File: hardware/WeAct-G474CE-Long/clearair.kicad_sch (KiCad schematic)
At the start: 40 parts, among them J1 220VAC mains in, M1 AC vent fan, M2 40mm fan (5V or 12V), Q1 2N7000, Q2 2N7000, Q3 2N2222A, Q4 IRFZ44N, Q5 AO3400A, SW1 RESET, SW2 COLD_BOOT, U1 SPS30, U2 BME680, U3 MQ131, U4 MiCS-4514, U5 RobotDyn AC dimmer, U6 PCF8563 RTC

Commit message: define the buzzer cycle
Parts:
- removed Q4: IRFZ44N, Package_TO_SOT_THT:TO-220-3_Vertical, symbol Transistor_FET:IRLZ44N
- removed R16: 10k, symbol Device:R
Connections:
- net at Q3.3 (C): now also BZ1.2 (-)
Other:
- note added: "Buzzer: PB15 (BUZZER_IN) -> R9 1k -> Q3 2N2222A base. Q3 switches the 12V buzzer on its low side: PB15 HIGH -> buzzer ON, LOW -> OFF. MiCS-4514 PRE tied to GND (boost not used). PB12 (MQ131_PREHEAT) -> R17 100R -> Q5 AO3400A gate, R18 100k pull-down: low-side switch in the MQ131 GND, HIGH = heater on. Cold/warm boot button SW2 -> PB14 (BOOT_MODE, pull-up). Gate PB1 (TRIAC_DIMMER) -> RobotDyn PSM."
- note removed: "Buzzer: PB15 (BUZZER_IN) -> R9 -> Q3. Q3 inverts: PB15 HIGH -> buzzer OFF; LOW -> R16 pulls IRFZ44N gate to 12V -> buzzer ON. MiCS-4514 PRE tied to GND (boost not used). PB12 (MQ131_PREHEAT) -> R17 100R -> Q5 AO3400A gate, R18 100k pull-down: low-side switch in the MQ131 GND, HIGH = heater on. Cold/warm boot button SW2 -> PB14 (BOOT_MODE, pull-up). Gate PB1 (TRIAC_DIMMER) -> RobotDyn PSM."
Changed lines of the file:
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@@
 		(pin "3")
 		(instances (project "clearair" (path "/953560a5-36cf-5251-8f8d-509802d70a69" (reference "Q3") (unit 1)))))
-	(symbol (lib_id "Device:R") (at 193.04 86.36 180) (unit 1)
-		(exclude_from_sim no) (in_bom yes) (on_board yes) (dnp no)
-		(property "Reference" "R16" (at 195.072 86.36 90) (effects (font (size 1.27 1.27))))
-		(property "Value" "10k" (at 193.04 86.36 90) (effects (font (size 1.27 1.27))))
-		(property "Footprint" "" (at 194.818 86.36 90) (effects (font (size 1.27 1.27)) (hide yes)))
-		(property "Datasheet" "" (at 193.04 86.36 0) (effects (font (size 1.27 1.27)) (hide yes)))
-		(property "Description" "Resistor" (at 193.04 86.36 0) (effects (font (size 1.27 1.27)) (hide yes)))
-		(property "ki_keywords" "R res resistor" (at 193.04 86.36 0) (effects (font (size 1.27 1.27)) (hide yes)))
-		(property "ki_fp_filters" "R_*" (at 193.04 86.36 0) (effects (font (size 1.27 1.27)) (hide yes)))
-		(pin "1")
-		(pin "2")
-		(instances (project "clearair" (path "/953560a5-36cf-5251-8f8d-509802d70a69" (reference "R16") (unit 1)))))
-	(symbol (lib_id "Transistor_FET:IRLZ44N") (at 205.74 76.2 0) (unit 1)
-		(exclude_from_sim no) (in_bom yes) (on_board yes) (dnp no)
-		(property "Reference" "Q4" (at 210.82 74.295 0) (effects (font (size 1.27 1.27))))
-		(property "Value" "IRFZ44N" (at 210.82 76.2 0) (effects (font (size 1.27 1.27))))
-		(property "Footprint" "Package_TO_SOT_THT:TO-220-3_Vertical" (at 210.82 78.105 0) (effects (font (size 1.27 1.27)) (hide yes)))
-		(property "Datasheet" "http://www.irf.com/product-info/datasheets/data/irlz44n.pdf" (at 210.82 80.01 0) (effects (font (size 1.27 1.27)) (hide yes)))
-		(property "Description" "47A Id, 55V Vds, 22mOhm Rds Single N-Channel HEXFET Power MOSFET, TO-220AB" (at 205.74 76.2 0) (effects (font (size 1.27 1.27)) (hide yes)))
-		(property "ki_keywords" "N-Channel HEXFET MOSFET Logic-Level" (at 205.74 76.2 0) (effects (font (size 1.27 1.27)) (hide yes)))
-		(property "ki_fp_filters" "TO?220*" (at 205.74 76.2 0) (effects (font (size 1.27 1.27)) (hide yes)))
-		(pin "1")
-		(pin "2")
-		(pin "3")
-		(instances (project "clearair" (path "/953560a5-36cf-5251-8f8d-509802d70a69" (reference "Q4") (unit 1)))))
 	(symbol (lib_id "Device:Buzzer") (at 213.36 63.5 0) (unit 1)
 		(exclude_from_sim no) (in_bom yes) (on_board yes) (dnp no)
@@
 	(wire (pts (xy 281.94 299.72) (xy 281.94 223.52)) (stroke (width 0) (type default)))
 	(wire (pts (xy 177.8 76.2) (xy 173.99 76.2)) (stroke (width 0) (type default)))
-	(wire (pts (xy 193.04 82.55) (xy 193.04 76.2)) (stroke (width 0) (type default)))
-	(wire (pts (xy 193.04 76.2) (xy 193.04 69.85)) (stroke (width 0) (type default)))
-	(wire (pts (xy 193.04 69.85) (xy 185.42 69.85)) (stroke (width 0) (type default)))
-	(wire (pts (xy 185.42 69.85) (xy 185.42 71.12)) (stroke (width 0) (type default)))
-	(wire (pts (xy 200.66 76.2) (xy 193.04 76.2)) (stroke (width 0) (type default)))
-	(wire (pts (xy 208.28 71.12) (xy 208.28 66.04)) (stroke (width 0) (type default)))
-	(wire (pts (xy 208.28 66.04) (xy 210.82 66.04)) (stroke (width 0) (type default)))
 	(wire (pts (xy 345.44 172.72) (xy 345.44 181.61)) (stroke (width 0) (type default)))
 	(wire (pts (xy 345.44 181.61) (xy 345.44 182.88)) (stroke (width 0) (type default)))
@@
 	(wire (pts (xy 482.6 60.96) (xy 482.6 68.58)) (stroke (width 0) (type default)))
 	(wire (pts (xy 482.6 68.58) (xy 477.52 68.58)) (stroke (width 0) (type default)))
-	(wire (pts (xy 193.04 90.17) (xy 193.04 101.6)) (stroke (width 0) (type default)))
 	(wire (pts (xy 256.54 81.28) (xy 256.54 101.6)) (stroke (width 0) (type default)))
 	(wire (pts (xy 210.82 60.96) (xy 198.12 60.96)) (stroke (width 0) (type default)))
@@
 	(wire (pts (xy 266.7 83.82) (xy 266.7 106.68)) (stroke (width 0) (type default)))
 	(wire (pts (xy 185.42 81.28) (xy 185.42 106.68)) (stroke (width 0) (type default)))
-	(wire (pts (xy 208.28 81.28) (xy 208.28 106.68)) (stroke (width 0) (type default)))
 	(wire (pts (xy 302.26 299.72) (xy 302.26 294.64)) (stroke (width 0) (type default)))
 	(wire (pts (xy 302.26 294.64) (xy 311.15 294.64)) (stroke (width 0) (type default)))
@@
 	(wire (pts (xy 480.06 259.08) (xy 480.06 327.66)) (stroke (width 0) (type default)))
 	(wire (pts (xy 482.6 259.08) (xy 480.06 259.08)) (stroke (width 0) (type default)))
-	(junction (at 193.04 101.6) (diameter 0) (color 0 0 0 0))
 	(junction (at 198.12 101.6) (diameter 0) (color 0 0 0 0))
 	(junction (at 256.54 101.6) (diameter 0) (color 0 0 0 0))
@@
 	(junction (at 313.69 241.3) (diameter 0) (color 0 0 0 0))
 	(junction (at 185.42 106.68) (diameter 0) (color 0 0 0 0))
-	(junction (at 208.28 106.68) (diameter 0) (color 0 0 0 0))
 	(junction (at 266.7 106.68) (diameter 0) (color 0 0 0 0))
 	(junction (at 341.63 106.68) (diameter 0) (color 0 0 0 0))
@@
 	(junction (at 259.08 180.34) (diameter 0) (color 0 0 0 0))
 	(junction (at 226.06 182.88) (diameter 0) (color 0 0 0 0))
-	(junction (at 193.04 76.2) (diameter 0) (color 0 0 0 0))
 	(junction (at 345.44 181.61) (diameter 0) (color 0 0 0 0))
 	(junction (at 363.22 185.42) (diameter 0) (color 0 0 0 0))
@@
 	(text "I2C1: PA15 SCL / PB7 SDA. SPS30 SEL=GND (I2C, 0x69); BME680 SDO=3V3 (0x77), CS=3V3; PCF8563 RTC HW-689 (0x51, CR1220, COT and INT unused). 4k7 pull-ups to 3V3." (exclude_from_sim no) (at 25.4 345.44 0) (effects (font (size 1.27 1.27)) (justify left top)))
 	(text "5V outputs -> 1k8 (series) / 3k3 (to GND) divider -> 3.24V max at MCU pin:\nMQ131 AO -> PA0 (ADC1_IN1), MiCS RED -> PA1 (ADC2_IN2), MiCS NOX -> PA7 (ADC2_IN4), RobotDyn Z-C -> PB0 (EXTI0)." (exclude_from_sim no) (at 25.4 350.52 0) (effects (font (size 1.27 1.27)) (justify left top)))
-	(text "Buzzer: PB15 (BUZZER_IN) -> R9 -> Q3. Q3 inverts: PB15 HIGH -> buzzer OFF; LOW -> R16 pulls IRFZ44N gate to 12V -> buzzer ON.\nMiCS-4514 PRE tied to GND (boost not used). PB12 (MQ131_PREHEAT) -> R17 100R -> Q5 AO3400A gate, R18 100k pull-down: low-side switch in the MQ131 GND, HIGH = heater on. Cold/warm boot button SW2 -> PB14 (BOOT_MODE, pull-up). Gate PB1 (TRIAC_DIMMER) -> RobotDyn PSM." (exclude_from_sim no) (at 25.4 358.14 0) (effects (font (size 1.27 1.27)) (justify left top)))
+	(text "Buzzer: PB15 (BUZZER_IN) -> R9 1k -> Q3 2N2222A base. Q3 switches the 12V buzzer on its low side: PB15 HIGH -> buzzer ON, LOW -> OFF.\nMiCS-4514 PRE tied to GND (boost not used). PB12 (MQ131_PREHEAT) -> R17 100R -> Q5 AO3400A gate, R18 100k pull-down: low-side switch in the MQ131 GND, HIGH = heater on. Cold/warm boot button SW2 -> PB14 (BOOT_MODE, pull-up). Gate PB1 (TRIAC_DIMMER) -> RobotDyn PSM." (exclude_from_sim no) (at 25.4 358.14 0) (effects (font (size 1.27 1.27)) (justify left top)))
 	(text "J2 = STLINK-V3MINIE STDC14: 3 T_VCC, 4 SWDIO, 5/7/11 GND, 6 SWCLK, 12 T_NRST, 13 T_VCP_RX, 14 T_VCP_TX; 1/2/8/9/10 unused.\nSWD goes to the board P5 header (SWCLK/SWDIO/3V3/GND). USART2 VCP: PA2 TX -> T_VCP_TX, PA3 RX <- T_VCP_RX.\nUSART3 (future Arduino link): PB10 TX / PB11 RX through 2N7000 level shifters Q1/Q2." (exclude_from_sim no) (at 25.4 365.76 0) (effects (font (size 1.27 1.27)) (justify left top)))
 	(text "220VAC mains split: J1 -> RobotDyn TRIAC (fan) and PS1 AC-DC (12V buzzer, 5V board + peripherals).\nPS1 pins: 1 L, 2 N, 3 +12V, 4 +5V, 5 GND. M2 40mm fan runs all the time. JP1: bridge 1-2 for a 5V fan, 2-3 for a 12V fan." (exclude_from_sim no) (at 25.4 375.92 0) (effects (font (size 1.27 1.27)) (justify left top)))
@@
 	(junction (at 388.62 215.9) (diameter 0) (color 0 0 0 0))
 	(junction (at 367.03 201.93) (diameter 0) (color 0 0 0 0))
+	(wire (pts (xy 185.42 71.12) (xy 185.42 66.04)) (stroke (width 0) (type default)))
+	(wire (pts (xy 185.42 66.04) (xy 210.82 66.04)) (stroke (width 0) (type default)))
 	(sheet_instances (path "/" (page "1")))
 	(embedded_fonts no)

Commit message: REMOVE PB12 and update files
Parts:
- removed JP1: FAN_V_SEL, symbol Jumper:Jumper_3_Open
- removed M2: 40mm fan (5V or 12V), symbol Motor:Fan
- removed Q5: AO3400A, Package_TO_SOT_SMD:SOT-23, symbol Transistor_FET:AO3400A
- removed R17: 100, symbol Device:R
- removed R18: 100k, symbol Device:R
- added M2: 80mm fan front, Connector_PinHeader_2.54mm:PinHeader_1x04_P2.54mm_Vertical, symbol Connector_Generic:Conn_01x04
- added M3: 80mm fan rear, Connector_PinHeader_2.54mm:PinHeader_1x04_P2.54mm_Vertical, symbol Connector_Generic:Conn_01x04
- added R19, R20: 1k, Resistor_THT:R_Axial_DIN0207_L6.3mm_D2.5mm_P7.62mm_Horizontal, symbol Device:R
- added R21, R22: 10k, Resistor_THT:R_Axial_DIN0207_L6.3mm_D2.5mm_P7.62mm_Horizontal, symbol Device:R
- BZ1: footprint (none) -> Connector_PinHeader_2.54mm:PinHeader_1x02_P2.54mm_Vertical
- J: footprint (none) -> Connector_PinHeader_1.27mm:PinHeader_2x07_P1.27mm_Vertical
- J1, M1: footprint (none) -> TerminalBlock_Phoenix:TerminalBlock_Phoenix_MKDS-1,5-2-5.08_1x02_P5.08mm_Horizontal
- PS1: value AC-DC PSU 220VAC -> 12V / 5V -> AC-DC PSUs 12V 2A + 5V 2A (DC out); footprint (none) -> libraries:PSU_DC_12V_5V_Inputs
- R1, R10, R11, R12, R13, R14, R15, R2, R3, R4, R5, R6, R7, R8, R9: footprint (none) -> Resistor_THT:R_Axial_DIN0207_L6.3mm_D2.5mm_P7.62mm_Horizontal
- SW1, SW2: footprint (none) -> Button_Switch_THT:SW_PUSH_6mm
- U5: footprint (none) -> libraries:RobotDyn_Dimmer_Logic
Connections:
- net +12V: now also M2.2 (Pin_2), M3.2 (Pin_2)
- net +3V3: now also R21.1, R22.1
- net GND: now also U3.2 (GND), M2.1 (Pin_1), M3.1 (Pin_1)
- net at A.14 (PA9): now also R20.2
- net at A.15 (PA8): now also R19.2
- net at A.30 (PA5): now also M2.3 (Pin_3), R21.2
- net at A.7 (PB3): now also M3.3 (Pin_3), R22.2
- new net: M3.4 (Pin_4), R20.1
- new net: M2.4 (Pin_4), R19.1
- no-connect marks 55 -> 52
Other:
- note added: "220VAC mains split: J1 -> RobotDyn TRIAC (fan) and two separate AC-DC supplies (12V 2A: buzzer + M2/M3 fans, 5V 2A: board + peripherals). Off board (on_board no): J1, M1 and the AC side of PS1 and U5, wired with 1.5 mm2 copper. PS1 pins: 1 L, 2 N, 3 +12V, 4 +5V, 5 GND; the DC pins go to two 2-pin headers. U5 logic pins 1-4 go to a 4-pin header. Fans M2 (front) and M3 (rear) are 12V 4-pin 80 mm: 1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"
- note added: "Buzzer: PB15 (BUZZER_IN) -> R9 1k -> Q3 2N2222A base. Q3 switches the 12V buzzer on its low side: PB15 HIGH -> buzzer ON, LOW -> OFF. MiCS-4514 PRE tied to GND (boost not used). MQ131 heater runs on a steady 5 V (VCC/GND straight to the rails, no switch); PB12 is unused. Cold/warm boot button SW2 -> PB14 (BOOT_MODE, pull-up). Gate PB1 (TRIAC_DIMMER) -> RobotDyn PSM."
- note removed: "220VAC mains split: J1 -> RobotDyn TRIAC (fan) and PS1 AC-DC (12V buzzer, 5V board + peripherals). PS1 pins: 1 L, 2 N, 3 +12V, 4 +5V, 5 GND. M2 40mm fan runs all the time. JP1: bridge 1-2 for a 5V fan, 2-3 for a 12V fan."
- note removed: "Buzzer: PB15 (BUZZER_IN) -> R9 1k -> Q3 2N2222A base. Q3 switches the 12V buzzer on its low side: PB15 HIGH -> buzzer ON, LOW -> OFF. MiCS-4514 PRE tied to GND (boost not used). PB12 (MQ131_PREHEAT) -> R17 100R -> Q5 AO3400A gate, R18 100k pull-down: low-side switch in the MQ131 GND, HIGH = heater on. Cold/warm boot button SW2 -> PB14 (BOOT_MODE, pull-up). Gate PB1 (TRIAC_DIMMER) -> RobotDyn PSM."

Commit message: remove onboard parts
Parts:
- removed U1: SPS30, libraries:SPS30, symbol FullModules:SPS30
- removed U2: BME680, libraries:BME680_Board, symbol FullModules:BME680_Board
- removed U3: MQ131, libraries:MQ131_FlyingFish, symbol FullModules:MQ131_FlyingFish
- removed U4: MiCS-4514, libraries:MICS4514_Module, symbol FullModules:MICS4514_Module
- added J3: SPS30 wire header (1 VDD, 2 SDA, 3 SCL, 4 SEL, 5 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, Connector_PinHeader_2.54mm:PinHeader_1x05_P2.54mm_Vertical, symbol Connector_Generic:Conn_01x05
- added J4: BME680 wire header (1 VCC, 2 GND, 3 SCL, 4 SDA, 5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, Connector_PinHeader_2.54mm:PinHeader_1x06_P2.54mm_Vertical, symbol Connector_Generic:Conn_01x06
- added J5: MQ131 wire header (1 VCC, 2 GND, 3 DO nc, 4 AO), Connector_PinHeader_2.54mm:PinHeader_1x04_P2.54mm_Vertical, symbol Connector_Generic:Conn_01x04
- added J6: MiCS-4514 wire header (1 VCC, 2 GND, 3 RED, 4 NOX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, Connector_PinHeader_2.54mm:PinHeader_1x05_P2.54mm_Vertical, symbol Connector_Generic:Conn_01x05
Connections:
- net +3V3: now also J4.1 (Pin_1), J4.5 (Pin_5), J4.6 (Pin_6)
- net +5V: now also J3.1 (Pin_1), J5.1 (Pin_1), J6.1 (Pin_1)
- net GND: now also J3.4 (Pin_4), J3.5 (Pin_5), J4.2 (Pin_2), J5.2 (Pin_2), J6.2 (Pin_2), J6.5 (Pin_5)
- net at A.10 (PA15), R1.2, U6.4 (SCL): now also J3.3 (Pin_3), J4.3 (Pin_3)
- net at A.3 (PB7), R2.2, U6.3 (SDA): now also J3.2 (Pin_2), J4.4 (Pin_4)
- net at R7.1: now also J6.4 (Pin_4)
- net at R5.2: now also J6.3 (Pin_3)
- net at R3.1: now also J5.4 (Pin_4)
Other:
- note added: "220VAC mains split: J1 -> RobotDyn TRIAC (fan) and two separate AC-DC supplies (12V 2A: buzzer + M2/M3 fans, 5V 2A: board + peripherals). Off board (on_board no): J1, M1 and the AC side of PS1 and U5, wired with 1.5 mm2 copper. The sensor modules (SPS30, BME680, MQ131, MiCS-4514) are off the PCB and are connected with wires to the PCB wire headers J3 (SPS30), J4 (BME680), J5 (MQ131) and J6 (MiCS-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"
- note removed: "220VAC mains split: J1 -> RobotDyn TRIAC (fan) and two separate AC-DC supplies (12V 2A: buzzer + M2/M3 fans, 5V 2A: board + peripherals). Off board (on_board no): J1, M1 and the AC side of PS1 and U5, wired with 1.5 mm2 copper. PS1 pins: 1 L, 2 N, 3 +12V, 4 +5V, 5 GND; the DC pins go to two 2-pin headers. U5 logic pins 1-4 go to a 4-pin header. Fans M2 (front) and M3 (rear) are 12V 4-pin 80 mm: 1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"

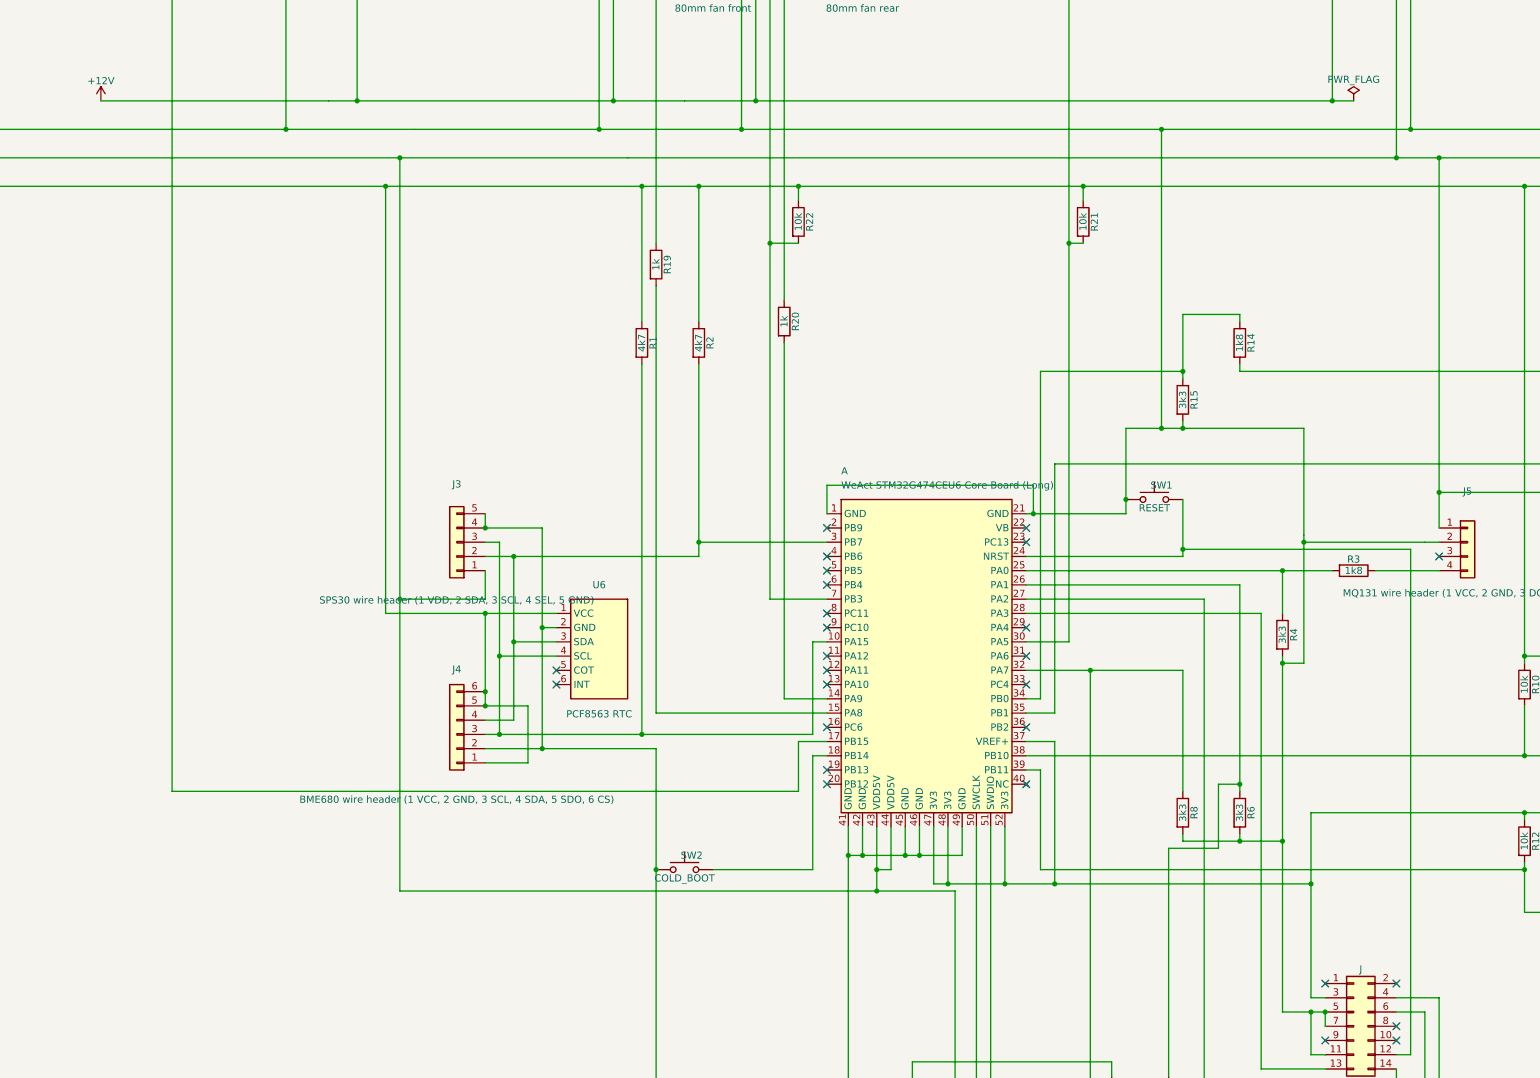
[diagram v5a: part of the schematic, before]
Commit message: validate all needed on the pcb
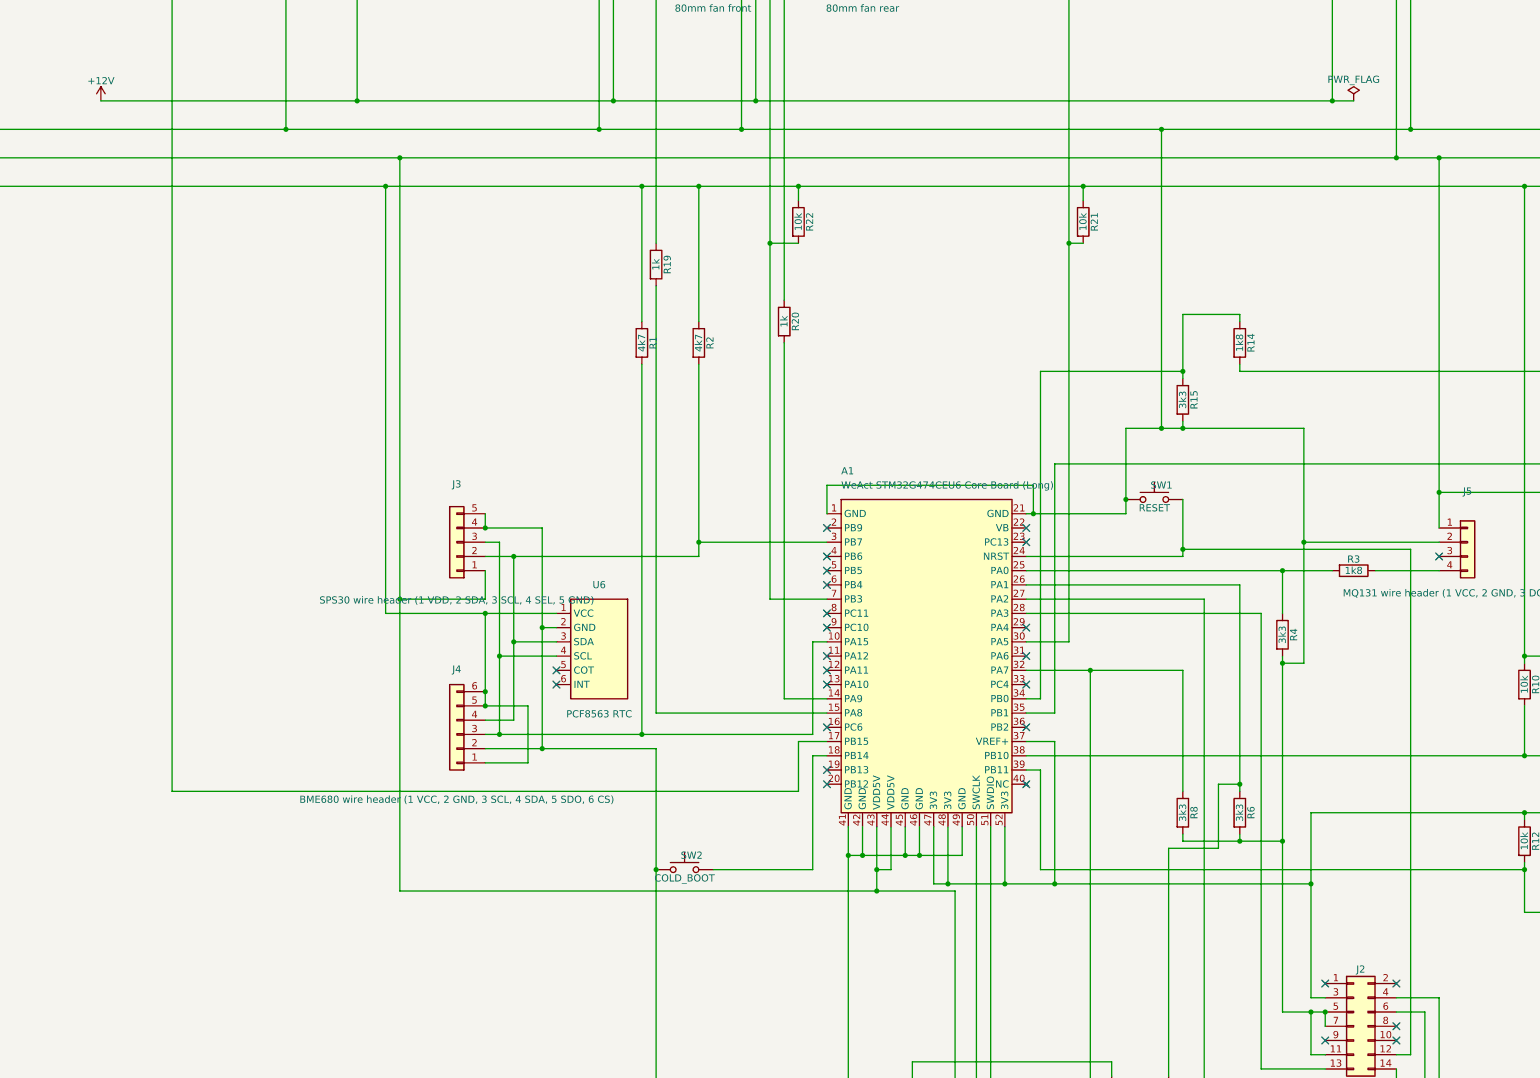
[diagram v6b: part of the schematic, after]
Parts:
- renumbered A to A1, J to J2

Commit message: change the layout for helping with the wires
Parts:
- Q1, Q2, Q3: footprint Package_TO_SOT_THT:TO-92_Inline -> Package_TO_SOT_THT:TO-92_Inline_Wide
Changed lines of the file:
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@@
 			)
 		)
-		(property "Footprint" "Package_TO_SOT_THT:TO-92_Inline"
+		(property "Footprint" "Package_TO_SOT_THT:TO-92_Inline_Wide"
 			(at 417.195 248.92 90)
 			(hide yes)
@@
 			)
 		)
-		(property "Footprint" "Package_TO_SOT_THT:TO-92_Inline"
+		(property "Footprint" "Package_TO_SOT_THT:TO-92_Inline_Wide"
 			(at 417.195 220.98 90)
 			(hide yes)
@@
 			)
 		)
-		(property "Footprint" "Package_TO_SOT_THT:TO-92_Inline"
+		(property "Footprint" "Package_TO_SOT_THT:TO-92_Inline_Wide"
 			(at 187.96 78.105 0)
 			(hide yes)
